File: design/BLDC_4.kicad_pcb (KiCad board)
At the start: 4 copper layers, 39.9 x 103.6 mm, 126 parts, among them J101 Conn_02x16_Odd_Even, J801 Conn_02x16_Odd_Even, J802 Conn_02x16_Odd_Even, J803 USB_C_Receptacle_USB2.0_16P, K801 SERVO, P4 IN+, P5 IN-, P6 MOTOR1, P7 MOTOR2, P801 SWD, P9 MOTOR3, Q1 IRFS7530, Q2 IRFS7530, Q3 IRFS7530, Q4 IRFS7530, Q5 IRFS7530, Q6 IRFS7530, U1 STM32F40X_LQFP64, U2 TC2117, U3 DRV8302, U401 SN65HVD232, X2 8MHz 10ppm, X801 MINI-USB-SHIELD-32005-201

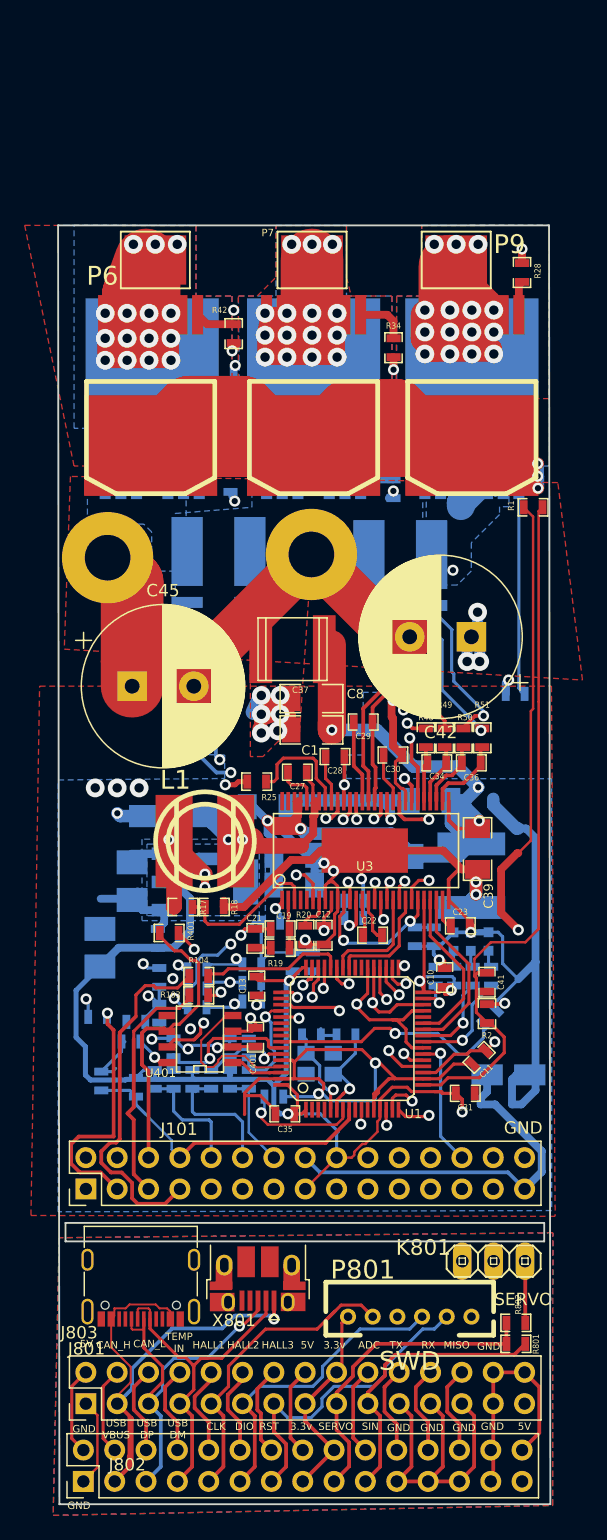
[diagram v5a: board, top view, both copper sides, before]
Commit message: v4.14 Changed power connectors to XT90 and XT60
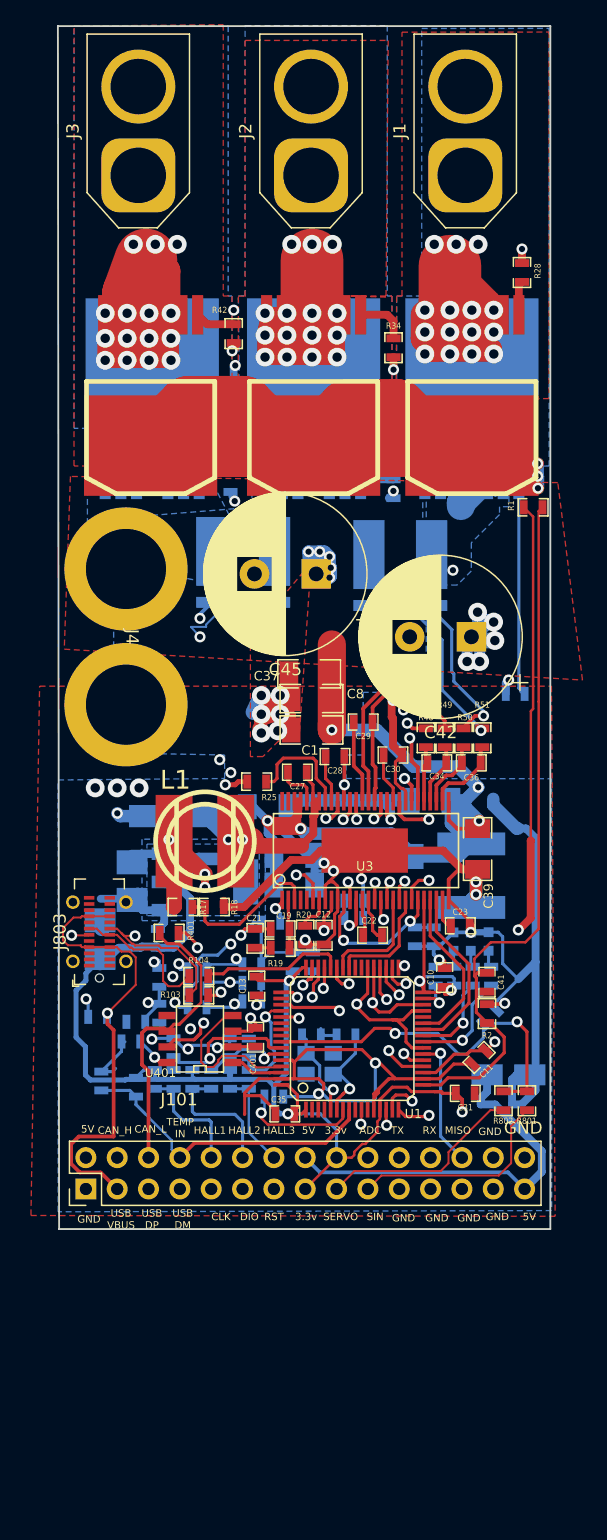
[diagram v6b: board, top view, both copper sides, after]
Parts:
- removed J801, J802: Conn_02x16_Odd_Even, Connector_PinHeader_2.54mm:PinHeader_2x15_P2.54mm_Vertical
- removed K801: SERVO, CRF1:pinhead-1X03
- removed P4: IN+, MountingHole:MountingHole_3.7mm_Pad
- removed P5: IN-, MountingHole:MountingHole_3.7mm_Pad
- removed P6: MOTOR1, CRF1:1PAD_4x5mm
- removed P7: MOTOR2, CRF1:1PAD_4x5mm
- removed P801: SWD, CRF1:MICRO_JST_6
- removed P9: MOTOR3, CRF1:1PAD_4x5mm
- removed X801: MINI-USB-SHIELD-32005-201, Connector_USB:USB_Micro-B_Amphenol_10103594-0001LF_Horizontal
- added J1: Conn_01x02_Pin, Connector_AMASS:AMASS_XT60-F_1x02_P7.20mm_Vertical, F.Cu at (110.0, 61.1)
- added J2: Conn_01x02_Pin, Connector_AMASS:AMASS_XT60-F_1x02_P7.20mm_Vertical, F.Cu at (97.5, 61.1)
- added J3: Conn_01x02_Pin, Connector_AMASS:AMASS_XT60-F_1x02_P7.20mm_Vertical, F.Cu at (83.5, 61.1)
- added J4: Conn_01x02_Pin, august:xt-90 vertical, F.Cu at (82.5, 98.5)
- C37: value 15u,100V -> 10u,50V; footprint w_smd_cap:c_2220 -> CRF1:SMD-1206
- C51: value 15u, 100v -> 15u,100V
- D3: value LED -> RED
- J803: footprint Connector_USB:USB_C_Receptacle_G-Switch_GT-USB-7010ASV -> Connector_USB:USB_C_Receptacle_GCT_USB4115-03-C
- R401: value NI -> 120R
- moved J803 27.9 mm to (80.3, 122.4), turned to 90 degrees
- moved R801 19.7 mm to (115.0, 136.1), turned to -90 degrees
- moved R802 18.0 mm to (113.1, 136.1), turned to -90 degrees
- moved C45 17.5 mm to (97.9, 93.4), turned to 180 degrees
- moved C37 2.41 mm to (97.3, 101.5), turned to 0 degrees
- moved R54 2.00 mm to (92.0, 94.6)
- moved C25 0.70 mm to (80.4, 123.0)
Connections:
- J101 pad 17: /SERVO_SIGNAL -> /SERVO_OUT
- J101 pad 19: unconnected-(J101-Pin_19-Pad19) -> /RC_PWM_INPUT
- J101 pad 5: /USB_DP -> /USB_VBUS
- J101 pad 7: /USB_DM -> /USB_VBUS
- J803 pad A1: /connboard/GND -> GND
- J803 pad A12: /connboard/GND -> GND
- J803 pad A4: /connboard/USB_VBUS -> /USB_VBUS
- J803 pad A6: /connboard/USB_DP -> /USB_DP
- J803 pad A7: /connboard/USB_DM -> /USB_DM
- J803 pad A9: /connboard/USB_VBUS -> /USB_VBUS
- J803 pad B1: /connboard/GND -> GND
- J803 pad B12: /connboard/GND -> GND
- J803 pad B4: /connboard/USB_VBUS -> /USB_VBUS
- J803 pad B6: /connboard/USB_DP -> /USB_DP
- J803 pad B7: /connboard/USB_DM -> /USB_DM
- J803 pad B9: /connboard/USB_VBUS -> /USB_VBUS
- J803 pad S1: /connboard/GND -> GND
- R801 pad 1: /connboard/SERVO_SIGNAL -> /SERVO_SIGNAL
- R801 pad 2: /connboard/SERVO_INPUT -> /RC_PWM_INPUT
- R802 pad 1: /connboard/SERVO_SIGNAL -> /SERVO_SIGNAL
- R802 pad 2: /connboard/SERVO_OUT -> /SERVO_OUT
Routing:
- net /connboard/GND: track 52.7 -> 0.00 mm
- net /connboard/USB_VBUS: track 48.7 -> 0.00 mm, vias 1 -> 0
- net /connboard/USB_DP: track 31.5 -> 0.00 mm, vias 1 -> 0
- net /connboard/USB_DM: track 31.2 -> 0.00 mm
- net /connboard/SWCLK: track 26.7 -> 0.00 mm
- net /connboard/NRST: track 25.9 -> 0.00 mm
- net /connboard/SERVO_SIGNAL: track 25.7 -> 0.00 mm
- net GND: track 320.5 -> 295.1 mm
- net /connboard/SWDIO: track 25.2 -> 0.00 mm
- net /connboard/SERVO_INPUT: track 23.0 -> 0.00 mm
- net /USB_VBUS: track 20.4 -> 43.1 mm
- net /USB_DM: track 29.1 -> 11.6 mm
- net /RC_PWM_INPUT: track 0.00 -> 17.3 mm
- net /connboard/VCC: track 16.8 -> 0.00 mm
- net /SERVO_OUT: track 0.00 -> 16.7 mm
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- removed copper zone on In2.Cu, net /connboard/5V
- removed copper zone on B.Cu, net /connboard/GND
- removed copper zone on F.Cu, net /connboard/GND
- removed copper zone on In1.Cu, net /connboard/GND
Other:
- board size 39.9 x 103.6 mm -> 39.9 x 97.5 mm

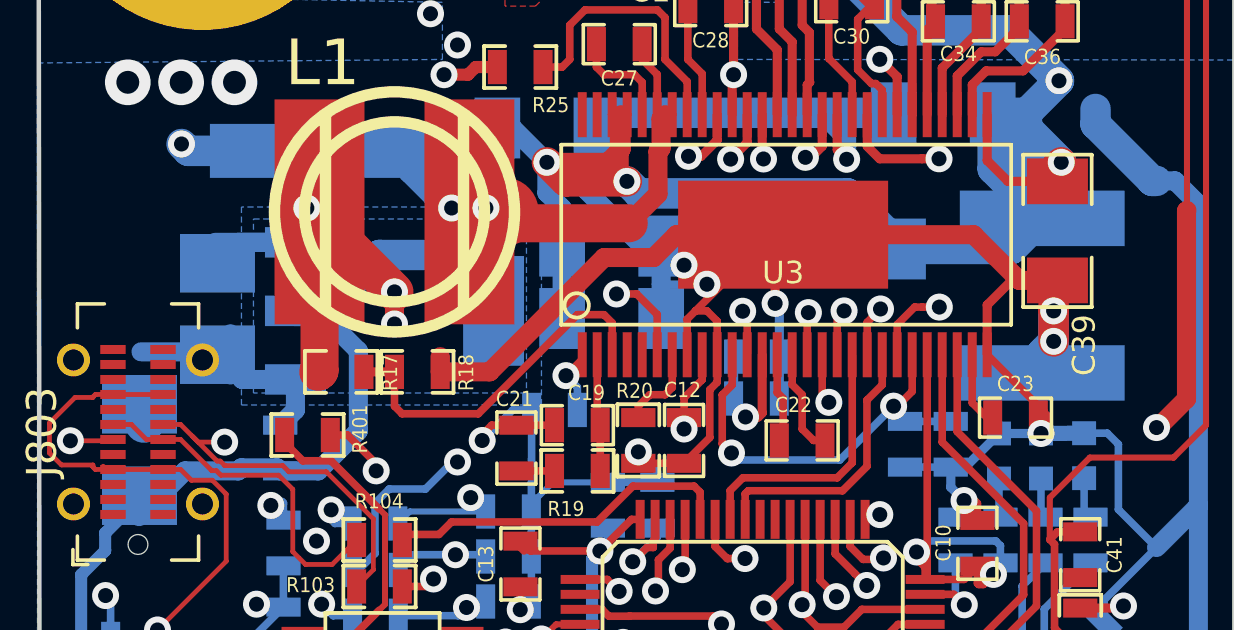
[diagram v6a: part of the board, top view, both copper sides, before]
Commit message: moved a cap to not interfere with the usb connector
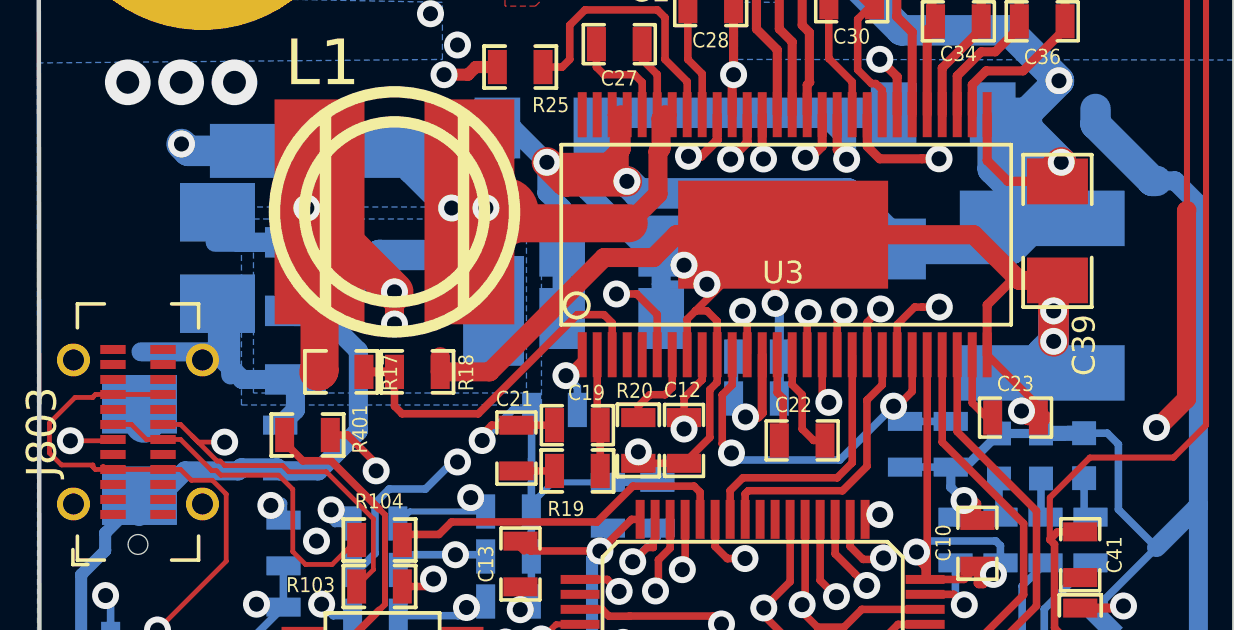
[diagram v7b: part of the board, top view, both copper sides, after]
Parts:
- moved C33 1.70 mm to (83.0, 116.6)
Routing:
- net GND: track 295.1 -> 299.6 mm
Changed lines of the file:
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@@
 		)
 	)
-	(property "version" "4.14")
+	(property "version" "4.15")
 	(net 0 "")
 	(net 1 "+5V")
@@
 		(model "${KICAD9_3DMODEL_DIR}/Connector_AMASS.3dshapes/AMASS_XT60-M_1x02_P7.2mm_Vertical.step"
 			(offset
-				(xyz -5.5 0 0)
+				(xyz 5 0 0)
 			)
 			(scale
@@
 			)
 			(rotate
-				(xyz -0 -0 -0)
+				(xyz -0 -0 -180)
 			)
 		)
@@
 	(footprint "w_smd_cap:c_tant_B"
 		(layer "B.Cu")
-		(at 83 118.3 90)
+		(at 83 116.6 90)
 		(descr "SMT capacitor, tantalum size B")
 		(property "Reference" "C33"
@@
 	)
 	(segment
-		(start 83.698 116.078)
-		(end 83 116.776)
-		(width 0.635)
-		(layer "B.Cu")
-		(net 1)
-	)
-	(segment
 		(start 113.4624 141.9024)
 		(end 98.2224 141.9024)
@@
 	)
 	(segment
+		(start 85.598 116.078)
+		(end 83.698 116.078)
+		(width 0.635)
+		(layer "B.Cu")
+		(net 1)
+	)
+	(segment
+		(start 83.698 116.078)
+		(end 83 115.38)
+		(width 0.635)
+		(layer "B.Cu")
+		(net 1)
+	)
+	(segment
 		(start 111.252 136.398)
 		(end 112.417795 136.398)
@@
 	)
 	(segment
+		(start 83 115.38)
+		(end 83 115.076)
+		(width 0.635)
+		(layer "B.Cu")
+		(net 1)
+	)
+	(segment
 		(start 79.438 128.021151)
 		(end 79.438 129.3)
@@
 	)
 	(segment
-		(start 85.598 116.078)
-		(end 83.698 116.078)
-		(width 0.635)
-		(layer "B.Cu")
-		(net 1)
-	)
-	(segment
 		(start 78.785 133.88626)
 		(end 79.25 134.35126)
@@
 	)
 	(segment
-		(start 110.449994 122.023506)
-		(end 110.449994 122.450703)
-		(width 0.508)
-		(layer "F.Cu")
-		(net 2)
-	)
-	(segment
 		(start 110.5535 121.92)
 		(end 110.5535 121.72188)
@@
 	)
 	(segment
+		(start 110.02 121.92)
+		(end 109.8 121.7)
+		(width 0.508)
+		(layer "F.Cu")
+		(net 2)
+	)
+	(segment
 		(start 98.528254 134.728158)
 		(end 98.528254 135.111765)
@@
 	)
 	(segment
-		(start 110.5535 121.92)
-		(end 110.449994 122.023506)
-		(width 0.508)
-		(layer "F.Cu")
-		(net 2)
-	)
-	(segment
 		(start 107.8738 134.3152)
 		(end 109.062185 133.126815)
@@
 	)
 	(segment
+		(start 110.5535 121.92)
+		(end 110.02 121.92)
+		(width 0.508)
+		(layer "F.Cu")
+		(net 2)
+	)
+	(segment
 		(start 90.241099 131.735)
 		(end 91.167 131.735)
@@
 	)
 	(via
-		(at 110.449994 122.450703)
+		(at 109.8 121.7)
 		(size 0.9)
 		(drill 0.5)
@@
 	)
 	(segment
-		(start 83.826 120.65)
-		(end 83 119.824)
-		(width 0.635)
-		(layer "B.Cu")
-		(net 2)
-	)
-	(segment
-		(start 82.90428 119.72828)
-		(end 83 119.824)
-		(width 0.635)
-		(layer "B.Cu")
-		(net 2)
-	)
-	(segment
 		(start 85.2 129.888)
 		(end 86.35 131.038)
@@
 	)
 	(segment
+		(start 83 119.63256)
+		(end 83 118.124)
+		(width 0.635)
+		(layer "B.Cu")
+		(net 2)
+	)
+	(segment
 		(start 107.6 125.238)
 		(end 107.761697 125.238)
@@
 	)
 	(segment
-		(start 110.449998 122.450703)
-		(end 110.449994 122.450703)
-		(width 0.3048)
-		(layer "B.Cu")
-		(net 2)
-	)
-	(segment
 		(start 84.49564 113.284)
 		(end 84.49564 113.24336)
@@
 	)
 	(segment
-		(start 110.450001 122.4507)
-		(end 110.449998 122.450703)
-		(width 0.3048)
+		(start 82.90428 119.72828)
+		(end 83 119.63256)
+		(width 0.635)
 		(layer "B.Cu")
 		(net 2)
@@
 	)
 	(segment
+		(start 83.826 120.65)
+		(end 83 119.824)
+		(width 0.635)
+		(layer "B.Cu")
+		(net 2)
+	)
+	(segment
 		(start 105.537 111.76)
 		(end 103.124 111.76)
@@
 	)
 	(segment
-		(start 85.598 120.65)
-		(end 83.826 120.65)
-		(width 0.635)
-		(layer "B.Cu")
-		(net 2)
-	)
-	(segment
 		(start 97.663 124.079)
 		(end 97.663 123.698)
@@
 	)
 	(segment
+		(start 80.45 119.72828)
+		(end 82.90428 119.72828)
+		(width 0.635)
+		(layer "B.Cu")
+		(net 2)
+	)
+	(segment
 		(start 114.554 136.398)
 		(end 115.697 135.255)
@@
 	)
 	(segment
+		(start 85.598 120.65)
+		(end 83.826 120.65)
+		(width 0.635)
+		(layer "B.Cu")
+		(net 2)
+	)
+	(segment
 		(start 93.472 121.666)
 		(end 92.841436 121.666)
@@
 	)
 	(segment
-		(start 80.45 119.72828)
-		(end 82.90428 119.72828)
-		(width 0.635)
+		(start 92.841436 121.666)
+		(end 91.823218 122.684218)
+		(width 0.254)
 		(layer "B.Cu")
 		(net 2)
 	)
 	(segment
-		(start 92.841436 121.666)
-		(end 91.823218 122.684218)
-		(width 0.254)
+		(start 83 119.824)
+		(end 83 118.124)
+		(width 0.635)
 		(layer "B.Cu")
 		(net 2)
@@
 	)
 	(segment
+		(start 110.450001 122.4507)
+		(end 110.450001 122.350001)
+		(width 0.3048)
+		(layer "B.Cu")
+		(net 2)
+	)
+	(segment
 		(start 97.79 116.205)
 		(end 97.79 117.475)
@@
 		(layer "B.Cu")
 		(net 2)
+	)
+	(segment
+		(start 110.450001 122.350001)
+		(end 109.8 121.7)
+		(width 0.3048)
+		(layer "B.Cu")
+		(net 2)

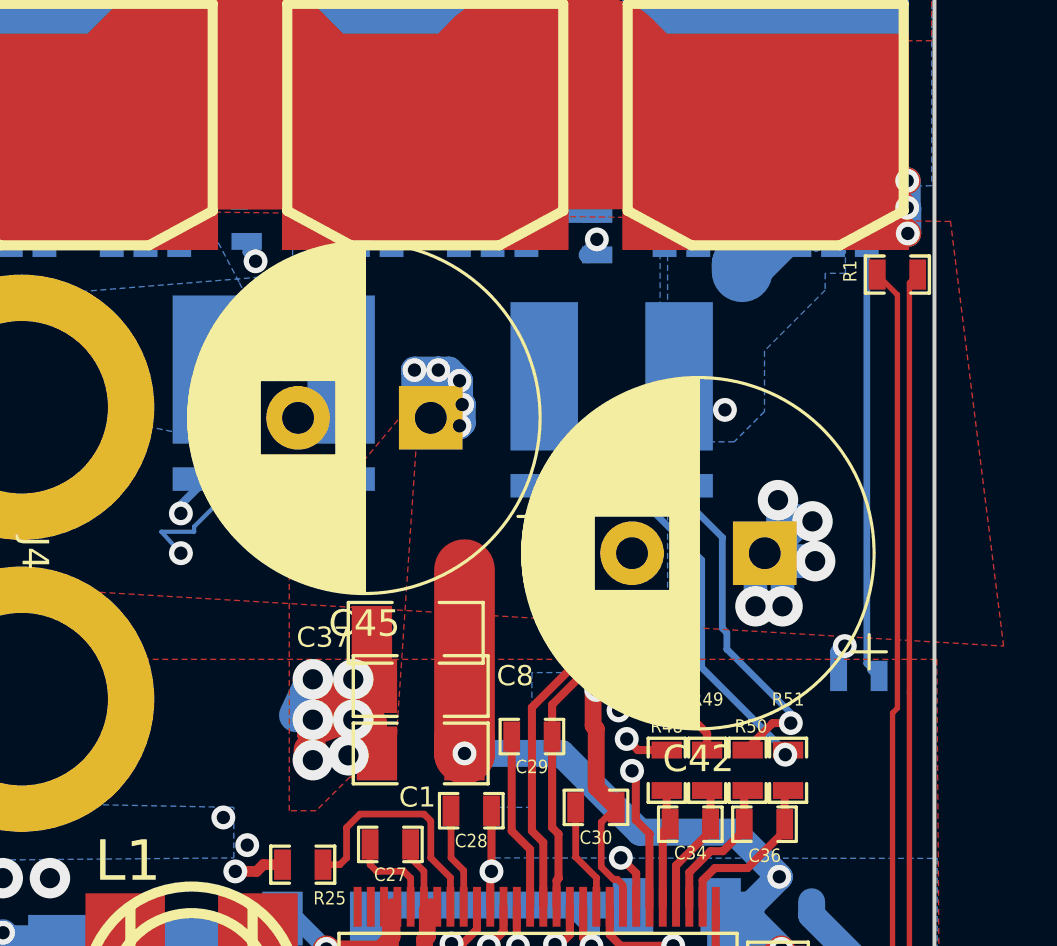
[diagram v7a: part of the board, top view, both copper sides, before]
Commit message: moved the big caps to not interfere with current sense shunts
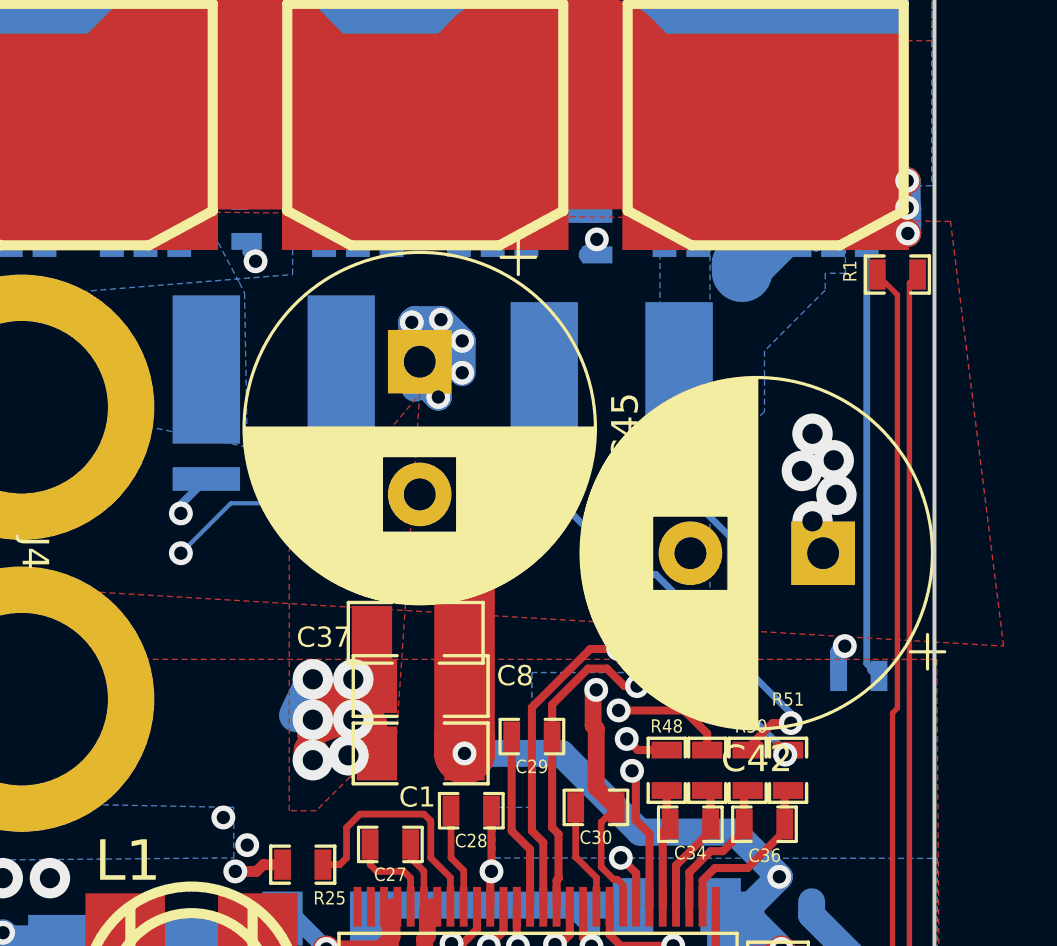
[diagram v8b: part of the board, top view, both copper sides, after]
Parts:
- moved C42 2.20 mm to (112.7, 98.5)
- moved C45 2.16 mm to (97.5, 91.3), turned to -90 degrees
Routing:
- net /Mosfet driver/M_L2: track 32.9 -> 34.8 mm
- net /Mosfet driver/SH1_B: track 40.0 -> 38.3 mm
- net /Mosfet driver/SH2_B: track 15.9 -> 14.7 mm
- net /Mosfet driver/H3_VS: track 174.8 -> 173.6 mm
- net /Mosfet driver/H1_LOW: track 46.7 -> 47.7 mm
- net V_SUPPLY: track 231.8 -> 232.8 mm
- net /Mosfet driver/H2_VS: track 159.0 -> 158.4 mm
- net /Mosfet driver/M_H1: track 63.8 -> 64.4 mm
